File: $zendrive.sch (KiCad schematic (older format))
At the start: 32 parts, among them CON1 BARREL_JACK, J1 JACK_INPUT, J2 JACK_OUTPUT, Q1 2N7000, Q2 2N7000, SW1 3PDT, U1 OPA2604

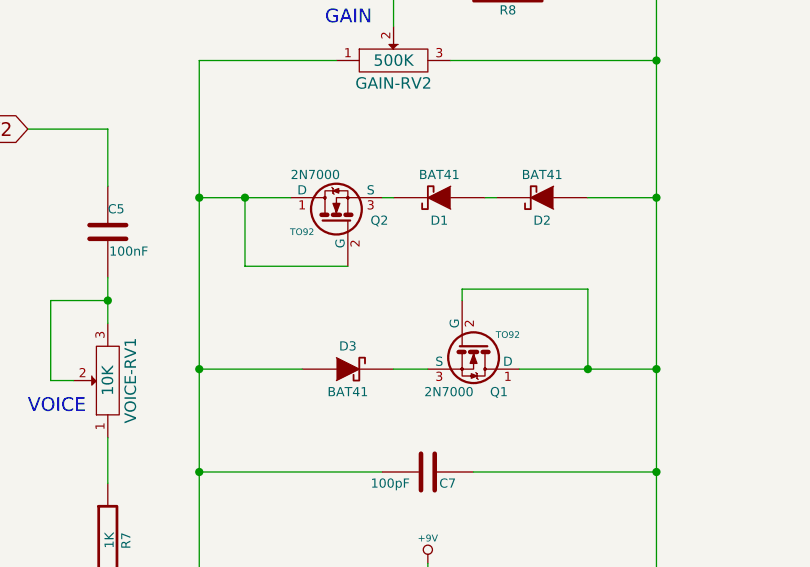
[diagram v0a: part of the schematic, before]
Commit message: Adding footprints
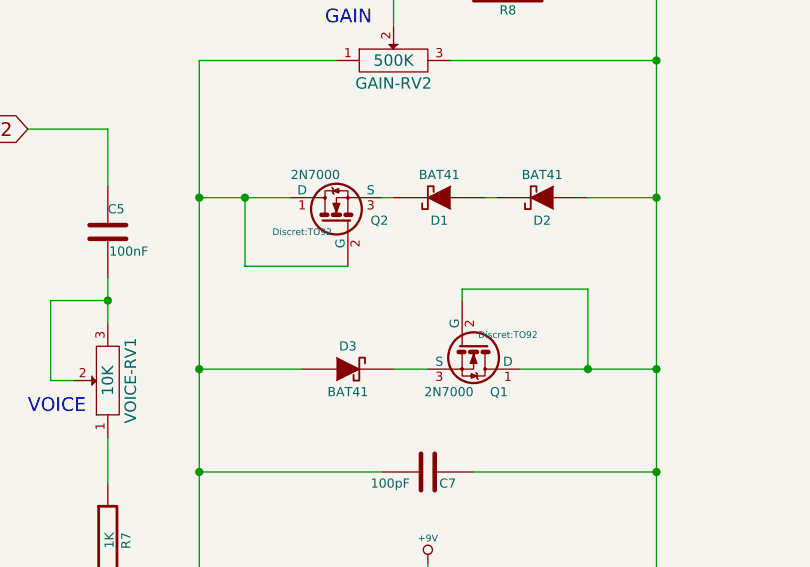
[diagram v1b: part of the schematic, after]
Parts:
- Q1, Q2: footprint TO92 -> Discret:TO92
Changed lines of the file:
@@
 F 0 "U1" H 3600 5650 60  0000 C CNN
 F 1 "OPA2604" H 3650 5300 60  0000 C CNN
-F 2 "" H 3450 5500 60  0000 C CNN
+F 2 "" H 3450 5500 60  0001 C CNN
 F 3 "" H 3450 5500 60  0000 C CNN
 	1    3450 5500
@@
 F 0 "U1" H 7000 5650 60  0000 C CNN
 F 1 "OPA2604" H 7050 5300 60  0000 C CNN
-F 2 "" H 6850 5500 60  0000 C CNN
+F 2 "" H 6850 5500 60  0001 C CNN
 F 3 "" H 6850 5500 60  0000 C CNN
 	2    6850 5500
@@
 $EndComp
 $Comp
-L +9V #PWR2
+L +9V #PWR01
 U 1 1 54AD8B1F
 P 1450 800
-F 0 "#PWR2" H 1450 770 20  0001 C CNN
+F 0 "#PWR01" H 1450 770 20  0001 C CNN
 F 1 "+9V" H 1450 910 30  0000 C CNN
 F 2 "" H 1450 800 60  0000 C CNN
@@
 $EndComp
 $Comp
-L GND #PWR3
+L GND #PWR02
 U 1 1 54AD8B5B
 P 1450 2150
-F 0 "#PWR3" H 1450 2150 30  0001 C CNN
+F 0 "#PWR02" H 1450 2150 30  0001 C CNN
 F 1 "GND" H 1450 2080 30  0001 C CNN
 F 2 "" H 1450 2150 60  0000 C CNN
@@
 F 0 "C1" H 1450 1550 40  0000 L CNN
 F 1 "100uF" H 1456 1365 40  0000 L CNN
-F 2 "" H 1488 1300 30  0000 C CNN
+F 2 "" H 1488 1300 30  0001 C CNN
 F 3 "" H 1450 1450 60  0000 C CNN
 	1    1450 1450
@@
 F 0 "C2" H 2400 1800 40  0000 L CNN
 F 1 "47uF" H 2406 1615 40  0000 L CNN
-F 2 "" H 2438 1550 30  0000 C CNN
+F 2 "" H 2438 1550 30  0001 C CNN
 F 3 "" H 2400 1700 60  0000 C CNN
 	1    2400 1700
@@
 F 0 "R1" V 2030 1100 40  0000 C CNN
 F 1 "10K" V 1957 1101 40  0000 C CNN
-F 2 "" V 1880 1100 30  0000 C CNN
+F 2 "" V 1880 1100 30  0001 C CNN
 F 3 "" H 1950 1100 30  0000 C CNN
 	1    1950 1100
@@
 F 0 "R2" V 2030 1700 40  0000 C CNN
 F 1 "10K" V 1957 1701 40  0000 C CNN
-F 2 "" V 1880 1700 30  0000 C CNN
+F 2 "" V 1880 1700 30  0001 C CNN
 F 3 "" H 1950 1700 30  0000 C CNN
 	1    1950 1700
@@
 F 0 "J1" H 7250 1800 60  0000 C CNN
 F 1 "JACK_INPUT" H 7450 2250 60  0000 C CNN
-F 2 "" H 7600 2000 60  0000 C CNN
+F 2 "" H 7600 2000 60  0001 C CNN
 F 3 "" H 7600 2000 60  0000 C CNN
 	1    7600 2000
@@
 F 0 "CON1" H 7650 1500 60  0000 C CNN
 F 1 "BARREL_JACK" H 7650 1050 60  0000 C CNN
-F 2 "" H 7650 1250 60  0000 C CNN
+F 2 "" H 7650 1250 60  0001 C CNN
 F 3 "" H 7650 1250 60  0000 C CNN
 	1    7650 1250
@@
 F 0 "BT1" H 6500 1550 50  0000 C CNN
 F 1 "BATTERY" H 6500 1160 50  0000 C CNN
-F 2 "" H 6500 1350 60  0000 C CNN
+F 2 "" H 6500 1350 60  0001 C CNN
 F 3 "" H 6500 1350 60  0000 C CNN
 	1    6500 1350
@@
 F 0 "C5" H 1950 3650 40  0000 L CNN
 F 1 "100nF" H 1956 3465 40  0000 L CNN
-F 2 "" H 1988 3400 30  0000 C CNN
+F 2 "" H 1988 3400 30  0001 C CNN
 F 3 "" H 1950 3550 60  0000 C CNN
 	1    1950 3550
@@
 F 0 "VOICE-RV1" H 1950 4100 50  0000 C CNN
 F 1 "10K" H 1950 4200 50  0000 C CNN
-F 2 "" H 1950 4200 60  0000 C CNN
+F 2 "" H 1950 4200 60  0001 C CNN
 F 3 "" H 1950 4200 60  0000 C CNN
 	1    1950 4200
@@
 F 0 "R7" V 2030 4900 40  0000 C CNN
 F 1 "1K" V 1957 4901 40  0000 C CNN
-F 2 "" V 1880 4900 30  0000 C CNN
+F 2 "" V 1880 4900 30  0001 C CNN
 F 3 "" H 1950 4900 30  0000 C CNN
 	1    1950 4900
@@
 $EndComp
 $Comp
-L GND #PWR5
+L GND #PWR03
 U 1 1 54ADA127
 P 3350 6050
-F 0 "#PWR5" H 3350 6050 30  0001 C CNN
+F 0 "#PWR03" H 3350 6050 30  0001 C CNN
 F 1 "GND" H 3350 5980 30  0001 C CNN
 F 2 "" H 3350 6050 60  0000 C CNN
@@
 $EndComp
 $Comp
-L +9V #PWR4
+L +9V #PWR04
 U 1 1 54ADA260
 P 3350 5000
-F 0 "#PWR4" H 3350 4970 20  0001 C CNN
+F 0 "#PWR04" H 3350 4970 20  0001 C CNN
 F 1 "+9V" H 3350 5110 30  0000 C CNN
 F 2 "" H 3350 5000 60  0000 C CNN
@@
 F 0 "C6" V 1800 5650 40  0000 L CNN
 F 1 "470nF" V 1800 5350 40  0000 L CNN
-F 2 "" H 1788 5450 30  0000 C CNN
+F 2 "" H 1788 5450 30  0001 C CNN
 F 3 "" H 1750 5600 60  0000 C CNN
 	1    1750 5600
@@
 F 0 "R6" V 1430 6100 40  0000 C CNN
 F 1 "2M" V 1357 6101 40  0000 C CNN
-F 2 "" V 1280 6100 30  0000 C CNN
+F 2 "" V 1280 6100 30  0001 C CNN
 F 3 "" H 1350 6100 30  0000 C CNN
 	1    1350 6100
@@
 F 0 "R5" V 2430 6100 40  0000 C CNN
 F 1 "470K" V 2357 6101 40  0000 C CNN
-F 2 "" V 2280 6100 30  0000 C CNN
+F 2 "" V 2280 6100 30  0001 C CNN
 F 3 "" H 2350 6100 30  0000 C CNN
 	1    2350 6100
@@
 $EndComp
 $Comp
-L GND #PWR1
+L GND #PWR05
 U 1 1 54ADA714
 P 1350 6500
-F 0 "#PWR1" H 1350 6500 30  0001 C CNN
+F 0 "#PWR05" H 1350 6500 30  0001 C CNN
 F 1 "GND" H 1350 6430 30  0001 C CNN
 F 2 "" H 1350 6500 60  0000 C CNN
@@
 F 0 "GAIN-RV2" H 3200 2700 50  0000 C CNN
 F 1 "500K" H 3200 2800 50  0000 C CNN
-F 2 "" H 3200 2800 60  0000 C CNN
+F 2 "" H 3200 2800 60  0001 C CNN
 F 3 "" H 3200 2800 60  0000 C CNN
 	1    3200 2800
@@
 F 0 "Q2" V 2950 3351 40  0000 R CNN
 F 1 "2N7000" V 3150 3700 40  0000 R CNN
-F 2 "TO92" V 2900 3650 29  0000 C CNN
+F 2 "Discret:TO92" V 2900 3650 29  0000 C CNN
 F 3 "" H 2950 3500 60  0000 C CNN
 	1    2950 3500
@@
 F 0 "Q1" V 3750 4200 40  0000 R CNN
 F 1 "2N7000" V 3750 4050 40  0000 R CNN
-F 2 "TO92" V 3500 4200 29  0000 C CNN
+F 2 "Discret:TO92" V 3500 4200 29  0000 C CNN
 F 3 "" H 3550 4050 60  0000 C CNN
 	1    3550 4050
@@
 F 0 "D1" H 3400 3500 40  0000 C CNN
 F 1 "BAT41" H 3400 3300 40  0000 C CNN
-F 2 "" H 3400 3400 60  0000 C CNN
+F 2 "" H 3400 3400 60  0001 C CNN
 F 3 "" H 3400 3400 60  0000 C CNN
 	1    3400 3400
@@
 F 0 "D2" H 3850 3500 40  0000 C CNN
 F 1 "BAT41" H 3850 3300 40  0000 C CNN
-F 2 "" H 3850 3400 60  0000 C CNN
+F 2 "" H 3850 3400 60  0001 C CNN
 F 3 "" H 3850 3400 60  0000 C CNN
 	1    3850 3400
@@
 F 0 "D3" H 3000 4250 40  0000 C CNN
 F 1 "BAT41" H 3000 4050 40  0000 C CNN
-F 2 "" H 3000 4150 60  0000 C CNN
+F 2 "" H 3000 4150 60  0001 C CNN
 F 3 "" H 3000 4150 60  0000 C CNN
 	1    3000 4150
@@
 F 0 "C7" V 3400 4650 40  0000 L CNN
 F 1 "100pF" V 3400 4350 40  0000 L CNN
-F 2 "" H 3388 4450 30  0000 C CNN
+F 2 "" H 3388 4450 30  0001 C CNN
 F 3 "" H 3350 4600 60  0000 C CNN
 	1    3350 4600
@@
 F 0 "R8" V 3780 2500 40  0000 C CNN
 F 1 "1K" V 3707 2501 40  0000 C CNN
-F 2 "" V 3630 2500 30  0000 C CNN
+F 2 "" V 3630 2500 30  0001 C CNN
 F 3 "" H 3700 2500 30  0000 C CNN
 	1    3700 2500
@@
 F 0 "R4" V 4780 5500 40  0000 C CNN
 F 1 "10K" V 4707 5501 40  0000 C CNN
-F 2 "" V 4630 5500 30  0000 C CNN
+F 2 "" V 4630 5500 30  0001 C CNN
 F 3 "" H 4700 5500 30  0000 C CNN
 	1    4700 5500
@@
 F 0 "TONE-RV3" H 5350 5400 50  0000 C CNN
 F 1 "50K" H 5350 5500 50  0000 C CNN
-F 2 "" H 5350 5500 60  0000 C CNN
+F 2 "" H 5350 5500 60  0001 C CNN
 F 3 "" H 5350 5500 60  0000 C CNN
 	1    5350 5500
@@
 F 0 "C4" H 5750 6200 40  0000 L CNN
 F 1 "3.3nF" H 5756 6015 40  0000 L CNN
-F 2 "" H 5788 5950 30  0000 C CNN
+F 2 "" H 5788 5950 30  0001 C CNN
 F 3 "" H 5750 6100 60  0000 C CNN
 	1    5750 6100
@@
 $EndComp
 $Comp
-L GND #PWR7
+L GND #PWR06
 U 1 1 54ADD108
 P 5750 6450
-F 0 "#PWR7" H 5750 6450 30  0001 C CNN
+F 0 "#PWR06" H 5750 6450 30  0001 C CNN
 F 1 "GND" H 5750 6380 30  0001 C CNN
 F 2 "" H 5750 6450 60  0000 C CNN
@@
 $EndComp
 $Comp
-L GND #PWR10
+L GND #PWR07
 U 1 1 54ADD542
 P 6750 6000
-F 0 "#PWR10" H 6750 6000 30  0001 C CNN
+F 0 "#PWR07" H 6750 6000 30  0001 C CNN
 F 1 "GND" H 6750 5930 30  0001 C CNN
 F 2 "" H 6750 6000 60  0000 C CNN
@@
 $EndComp
 $Comp
-L +9V #PWR9
+L +9V #PWR08
 U 1 1 54ADD727
 P 6750 5050
-F 0 "#PWR9" H 6750 5020 20  0001 C CNN
+F 0 "#PWR08" H 6750 5020 20  0001 C CNN
 F 1 "+9V" H 6750 5160 30  0000 C CNN
 F 2 "" H 6750 5050 60  0000 C CNN
@@
 F 0 "C3" V 7750 5550 40  0000 L CNN
 F 1 "470nF" V 7900 5550 40  0000 L CNN
-F 2 "" H 7838 5350 30  0000 C CNN
+F 2 "" H 7838 5350 30  0001 C CNN
 F 3 "" H 7800 5500 60  0000 C CNN
 	1    7800 5500
@@
 F 0 "R3" V 8480 5500 40  0000 C CNN
 F 1 "1K" V 8407 5501 40  0000 C CNN
-F 2 "" V 8330 5500 30  0000 C CNN
+F 2 "" V 8330 5500 30  0001 C CNN
 F 3 "" H 8400 5500 30  0000 C CNN
 	1    8400 5500
@@
 F 0 "VOLUME-RV4" H 8950 5650 50  0000 C CNN
 F 1 "100K" H 8950 5750 50  0000 C CNN
-F 2 "" H 8950 5750 60  0000 C CNN
+F 2 "" H 8950 5750 60  0001 C CNN
 F 3 "" H 8950 5750 60  0000 C CNN
 	1    8950 5750
@@
 $EndComp
 $Comp
-L GND #PWR13
+L GND #PWR09
 U 1 1 54ADE069
 P 8950 6150
-F 0 "#PWR13" H 8950 6150 30  0001 C CNN
+F 0 "#PWR09" H 8950 6150 30  0001 C CNN
 F 1 "GND" H 8950 6080 30  0001 C CNN
 F 2 "" H 8950 6150 60  0000 C CNN
@@
 OUTPUT
 $Comp
-L +9V #PWR11
+L +9V #PWR010
 U 1 1 54ADE79F
 P 7000 1100
-F 0 "#PWR11" H 7000 1070 20  0001 C CNN
+F 0 "#PWR010" H 7000 1070 20  0001 C CNN
 F 1 "+9V" H 7000 1210 30  0000 C CNN
 F 2 "" H 7000 1100 60  0000 C CNN
@@
 F 0 "J2" H 9750 1250 60  0000 C CNN
 F 1 "JACK_OUTPUT" H 9950 1700 60  0000 C CNN
-F 2 "" H 10100 1450 60  0000 C CNN
+F 2 "" H 10100 1450 60  0001 C CNN
 F 3 "" H 10100 1450 60  0000 C CNN
 	1    10100 1450
@@
 Connection ~ 6100 1350
 $Comp
-L GND #PWR8
+L GND #PWR011
 U 1 1 54ADFE38
 P 6100 2400
-F 0 "#PWR8" H 6100 2400 30  0001 C CNN
+F 0 "#PWR011" H 6100 2400 30  0001 C CNN
 F 1 "GND" H 6100 2330 30  0001 C CNN
 F 2 "" H 6100 2400 60  0000 C CNN
@@
 F 0 "SW1" H 6700 3650 60  0000 C CNN
 F 1 "3PDT" H 6450 3500 60  0000 C CNN
-F 2 "" H 6450 3250 60  0000 C CNN
+F 2 "" H 6450 3250 60  0001 C CNN
 F 3 "" H 6450 3250 60  0000 C CNN
 	1    6450 3800
@@
 $EndComp
 $Comp
-L GND #PWR6
+L GND #PWR012
 U 1 1 54ADB4F5
 P 5650 3400
-F 0 "#PWR6" H 5650 3400 30  0001 C CNN
+F 0 "#PWR012" H 5650 3400 30  0001 C CNN
 F 1 "GND" H 5650 3330 30  0001 C CNN
 F 2 "" H 5650 3400 60  0000 C CNN
@@
 F 0 "D4" H 7750 3450 50  0000 C CNN
 F 1 "LED" H 7750 3250 50  0000 C CNN
-F 2 "" H 7750 3350 60  0000 C CNN
+F 2 "" H 7750 3350 60  0001 C CNN
 F 3 "" H 7750 3350 60  0000 C CNN
 	1    7750 3350
@@
 F 0 "R9" V 7230 3350 40  0000 C CNN
 F 1 "1K" V 7157 3351 40  0000 C CNN
-F 2 "" V 7080 3350 30  0000 C CNN
+F 2 "" V 7080 3350 30  0001 C CNN
 F 3 "" H 7150 3350 30  0000 C CNN
 	1    7150 3350
@@
 	7400 3350 7550 3350
 $Comp
-L +9V #PWR12
+L +9V #PWR013
 U 1 1 54ADB96A
 P 8100 3200
-F 0 "#PWR12" H 8100 3170 20  0001 C CNN
+F 0 "#PWR013" H 8100 3170 20  0001 C CNN
 F 1 "+9V" H 8100 3310 30  0000 C CNN
 F 2 "" H 8100 3200 60  0000 C CNN
@@
 	9650 1450 9450 1450
 $Comp
-L GND #PWR14
+L GND #PWR014
 U 1 1 54AE048F
 P 9450 1800
-F 0 "#PWR14" H 9450 1800 30  0001 C CNN
+F 0 "#PWR014" H 9450 1800 30  0001 C CNN
 F 1 "GND" H 9450 1730 30  0001 C CNN
 F 2 "" H 9450 1800 60  0000 C CNN
